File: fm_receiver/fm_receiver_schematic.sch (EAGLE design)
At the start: 22 parts

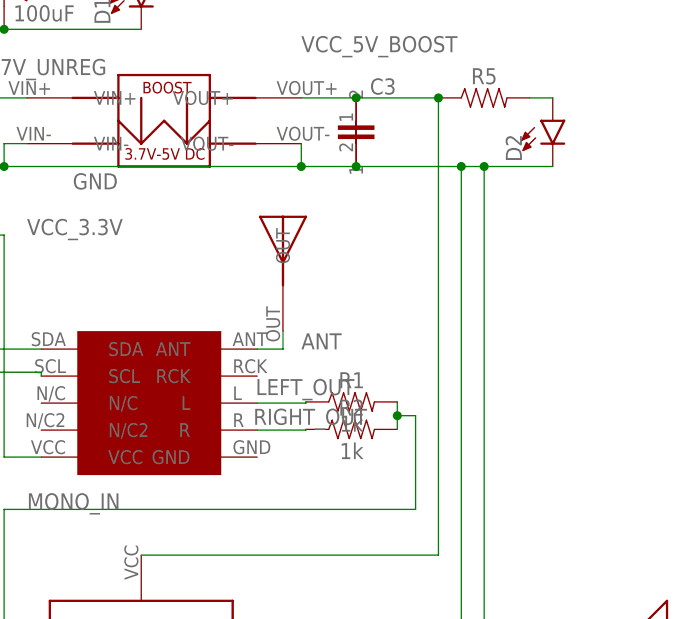
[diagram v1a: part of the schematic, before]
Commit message: connected crucial GND terminal of RDA5807 to GND net, which was previously missed
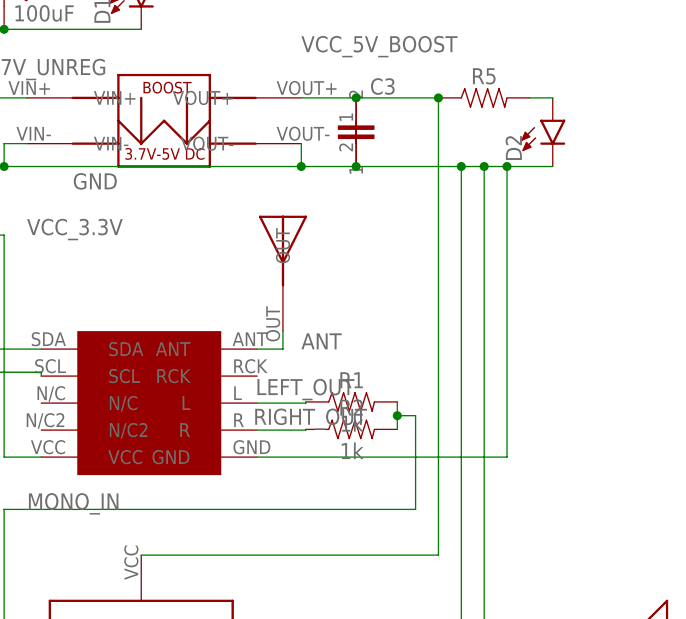
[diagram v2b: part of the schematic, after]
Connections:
- net GND: now also FM_RECEIVER.GND
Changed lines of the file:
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@@
 <grid distance="0.1" unitdist="inch" unit="inch" style="lines" multiple="1" display="no" altdistance="0.01" altunitdist="inch" altunit="inch"/>
 <layers>
-<layer number="1" name="Top" color="4" fill="1" visible="yes" active="no"/>
-<layer number="2" name="Route2" color="16" fill="1" visible="yes" active="no"/>
-<layer number="3" name="Route3" color="17" fill="1" visible="yes" active="no"/>
-<layer number="4" name="Route4" color="18" fill="1" visible="yes" active="no"/>
-<layer number="5" name="Route5" color="19" fill="1" visible="yes" active="no"/>
-<layer number="6" name="Route6" color="25" fill="1" visible="yes" active="no"/>
-<layer number="7" name="Route7" color="26" fill="1" visible="yes" active="no"/>
-<layer number="8" name="Route8" color="27" fill="1" visible="yes" active="no"/>
-<layer number="9" name="Route9" color="28" fill="1" visible="yes" active="no"/>
-<layer number="10" name="Route10" color="29" fill="1" visible="yes" active="no"/>
-<layer number="11" name="Route11" color="30" fill="1" visible="yes" active="no"/>
-<layer number="12" name="Route12" color="20" fill="1" visible="yes" active="no"/>
-<layer number="13" name="Route13" color="21" fill="1" visible="yes" active="no"/>
-<layer number="14" name="Route14" color="22" fill="1" visible="yes" active="no"/>
-<layer number="15" name="Route15" color="23" fill="1" visible="yes" active="no"/>
-<layer number="16" name="Bottom" color="1" fill="1" visible="yes" active="no"/>
-<layer number="17" name="Pads" color="2" fill="1" visible="yes" active="no"/>
-<layer number="18" name="Vias" color="2" fill="1" visible="yes" active="no"/>
-<layer number="19" name="Unrouted" color="6" fill="1" visible="yes" active="no"/>
-<layer number="20" name="Dimension" color="24" fill="1" visible="yes" active="no"/>
-<layer number="21" name="tPlace" color="7" fill="1" visible="yes" active="no"/>
-<layer number="22" name="bPlace" color="7" fill="1" visible="yes" active="no"/>
-<layer number="23" name="tOrigins" color="15" fill="1" visible="yes" active="no"/>
-<layer number="24" name="bOrigins" color="15" fill="1" visible="yes" active="no"/>
-<layer number="25" name="tNames" color="7" fill="1" visible="yes" active="no"/>
-<layer number="26" name="bNames" color="7" fill="1" visible="yes" active="no"/>
-<layer number="27" name="tValues" color="7" fill="1" visible="yes" active="no"/>
-<layer number="28" name="bValues" color="7" fill="1" visible="yes" active="no"/>
+<layer number="1" name="Top" color="4" fill="1" visible="no" active="no"/>
+<layer number="2" name="Route2" color="16" fill="1" visible="no" active="no"/>
+<layer number="3" name="Route3" color="17" fill="1" visible="no" active="no"/>
+<layer number="4" name="Route4" color="18" fill="1" visible="no" active="no"/>
+<layer number="5" name="Route5" color="19" fill="1" visible="no" active="no"/>
+<layer number="6" name="Route6" color="25" fill="1" visible="no" active="no"/>
+<layer number="7" name="Route7" color="26" fill="1" visible="no" active="no"/>
+<layer number="8" name="Route8" color="27" fill="1" visible="no" active="no"/>
+<layer number="9" name="Route9" color="28" fill="1" visible="no" active="no"/>
+<layer number="10" name="Route10" color="29" fill="1" visible="no" active="no"/>
+<layer number="11" name="Route11" color="30" fill="1" visible="no" active="no"/>
+<layer number="12" name="Route12" color="20" fill="1" visible="no" active="no"/>
+<layer number="13" name="Route13" color="21" fill="1" visible="no" active="no"/>
+<layer number="14" name="Route14" color="22" fill="1" visible="no" active="no"/>
+<layer number="15" name="Route15" color="23" fill="1" visible="no" active="no"/>
+<layer number="16" name="Bottom" color="1" fill="1" visible="no" active="no"/>
+<layer number="17" name="Pads" color="2" fill="1" visible="no" active="no"/>
+<layer number="18" name="Vias" color="2" fill="1" visible="no" active="no"/>
+<layer number="19" name="Unrouted" color="6" fill="1" visible="no" active="no"/>
+<layer number="20" name="Dimension" color="24" fill="1" visible="no" active="no"/>
+<layer number="21" name="tPlace" color="7" fill="1" visible="no" active="no"/>
+<layer number="22" name="bPlace" color="7" fill="1" visible="no" active="no"/>
+<layer number="23" name="tOrigins" color="15" fill="1" visible="no" active="no"/>
+<layer number="24" name="bOrigins" color="15" fill="1" visible="no" active="no"/>
+<layer number="25" name="tNames" color="7" fill="1" visible="no" active="no"/>
+<layer number="26" name="bNames" color="7" fill="1" visible="no" active="no"/>
+<layer number="27" name="tValues" color="7" fill="1" visible="no" active="no"/>
+<layer number="28" name="bValues" color="7" fill="1" visible="no" active="no"/>
 <layer number="29" name="tStop" color="7" fill="3" visible="no" active="no"/>
 <layer number="30" name="bStop" color="7" fill="6" visible="no" active="no"/>
@@
 <layer number="35" name="tGlue" color="7" fill="4" visible="no" active="no"/>
 <layer number="36" name="bGlue" color="7" fill="5" visible="no" active="no"/>
-<layer number="37" name="tTest" color="7" fill="1" visible="yes" active="no"/>
-<layer number="38" name="bTest" color="7" fill="1" visible="yes" active="no"/>
+<layer number="37" name="tTest" color="7" fill="1" visible="no" active="no"/>
+<layer number="38" name="bTest" color="7" fill="1" visible="no" active="no"/>
 <layer number="39" name="tKeepout" color="4" fill="11" visible="no" active="no"/>
 <layer number="40" name="bKeepout" color="1" fill="11" visible="no" active="no"/>
@@
 <layer number="44" name="Drills" color="7" fill="1" visible="no" active="no"/>
 <layer number="45" name="Holes" color="7" fill="1" visible="no" active="no"/>
-<layer number="46" name="Milling" color="3" fill="1" visible="yes" active="no"/>
-<layer number="47" name="Measures" color="7" fill="1" visible="yes" active="no"/>
-<layer number="48" name="Document" color="7" fill="1" visible="yes" active="no"/>
-<layer number="49" name="Reference" color="7" fill="1" visible="yes" active="no"/>
-<layer number="50" name="dxf" color="7" fill="1" visible="yes" active="no"/>
-<layer number="51" name="tDocu" color="7" fill="1" visible="yes" active="no"/>
-<layer number="52" name="bDocu" color="7" fill="1" visible="yes" active="no"/>
-<layer number="53" name="tGND_GNDA" color="7" fill="9" visible="yes" active="no"/>
-<layer number="54" name="bGND_GNDA" color="1" fill="9" visible="yes" active="no"/>
-<layer number="56" name="wert" color="7" fill="1" visible="yes" active="no"/>
-<layer number="57" name="tCAD" color="7" fill="1" visible="yes" active="no"/>
-<layer number="58" name="bCopper" color="7" fill="1" visible="yes" active="no"/>
-<layer number="59" name="tCarbon" color="7" fill="1" visible="yes" active="no"/>
-<layer number="60" name="bCarbon" color="7" fill="1" visible="yes" active="no"/>
+<layer number="46" name="Milling" color="3" fill="1" visible="no" active="no"/>
+<layer number="47" name="Measures" color="7" fill="1" visible="no" active="no"/>
+<layer number="48" name="Document" color="7" fill="1" visible="no" active="no"/>
+<layer number="49" name="Reference" color="7" fill="1" visible="no" active="no"/>
+<layer number="50" name="dxf" color="7" fill="1" visible="no" active="no"/>
+<layer number="51" name="tDocu" color="7" fill="1" visible="no" active="no"/>
+<layer number="52" name="bDocu" color="7" fill="1" visible="no" active="no"/>
+<layer number="53" name="tGND_GNDA" color="7" fill="9" visible="no" active="no"/>
+<layer number="54" name="bGND_GNDA" color="1" fill="9" visible="no" active="no"/>
+<layer number="56" name="wert" color="7" fill="1" visible="no" active="no"/>
+<layer number="57" name="tCAD" color="7" fill="1" visible="no" active="no"/>
+<layer number="58" name="bCopper" color="7" fill="1" visible="no" active="no"/>
+<layer number="59" name="tCarbon" color="7" fill="1" visible="no" active="no"/>
+<layer number="60" name="bCarbon" color="7" fill="1" visible="no" active="no"/>
 <layer number="88" name="SimResults" color="9" fill="1" visible="yes" active="yes"/>
 <layer number="89" name="SimProbes" color="9" fill="1" visible="yes" active="yes"/>
@@
 <junction x="50.8" y="43.18"/>
 <pinref part="D2" gate="D1" pin="C"/>
-<wire x1="111.76" y1="27.94" x2="104.14" y2="27.94" width="0.1524" layer="91"/>
+<wire x1="111.76" y1="27.94" x2="106.68" y2="27.94" width="0.1524" layer="91"/>
 <junction x="104.14" y="27.94"/>
-</segment>
-</net>
+<pinref part="FM_RECEIVER" gate="G$1" pin="GND"/>
+<wire x1="106.68" y1="27.94" x2="104.14" y2="27.94" width="0.1524" layer="91"/>
+<wire x1="78.928" y1="-4.348" x2="106.68" y2="-4.348" width="0.1524" layer="91"/>
+<wire x1="106.68" y1="-4.348" x2="106.68" y2="27.94" width="0.1524" layer="91"/>
+<junction x="106.68" y="27.94"/>
+</segment>
+</net>
